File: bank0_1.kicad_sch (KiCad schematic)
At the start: 1 part, among them U1 ECP5-BGA256

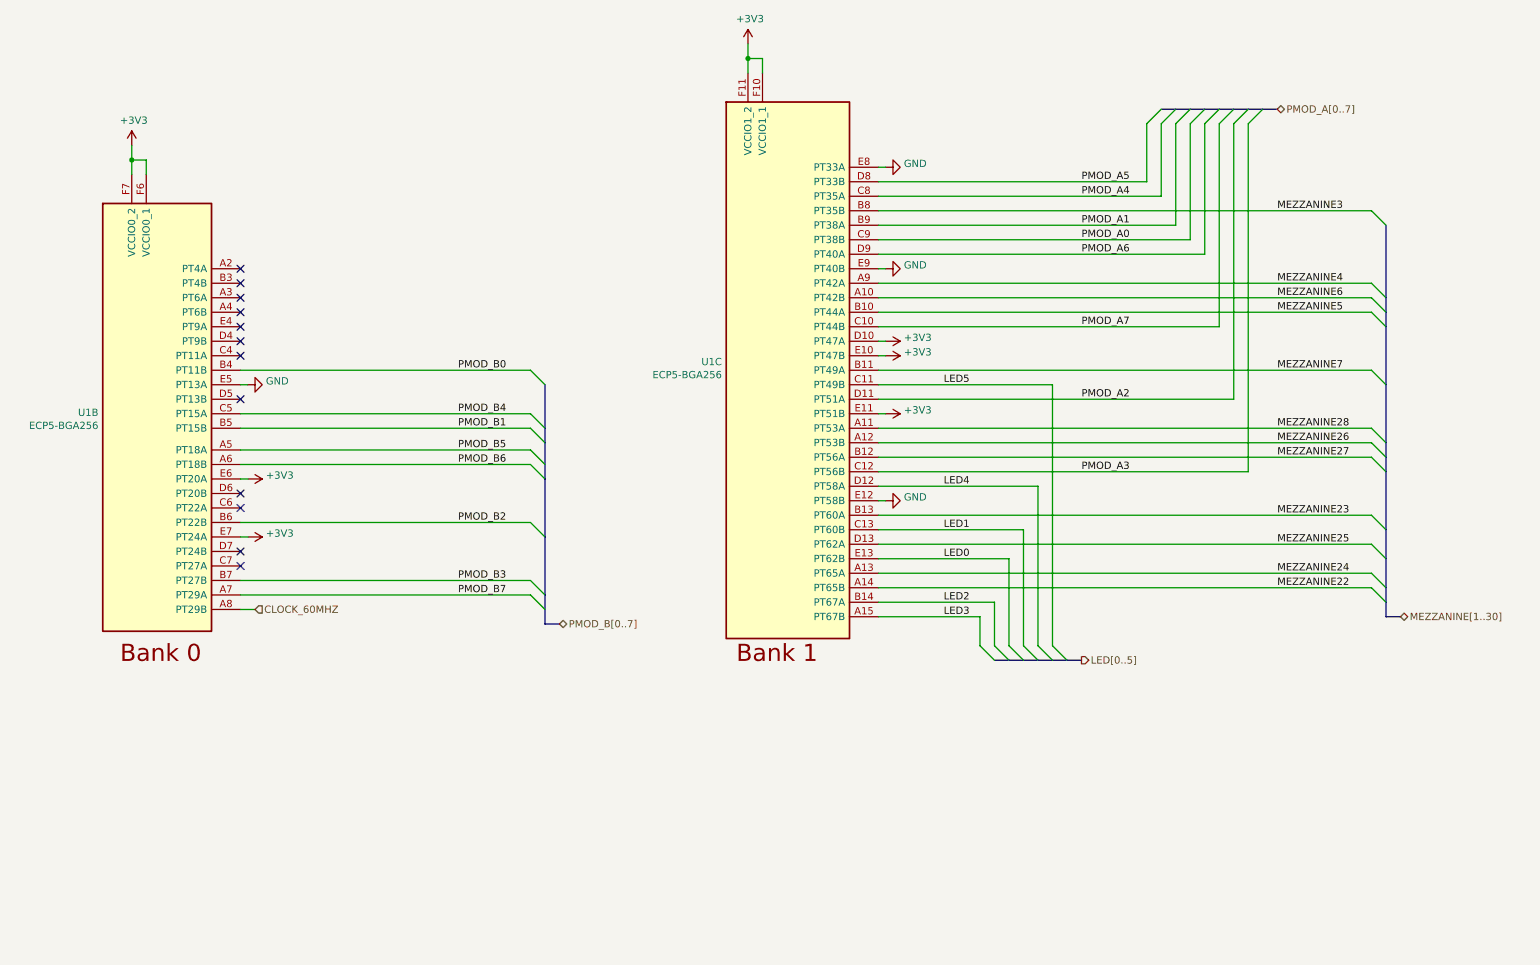
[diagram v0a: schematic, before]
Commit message: Add radio transceiver
Remove Cynthion-specific features
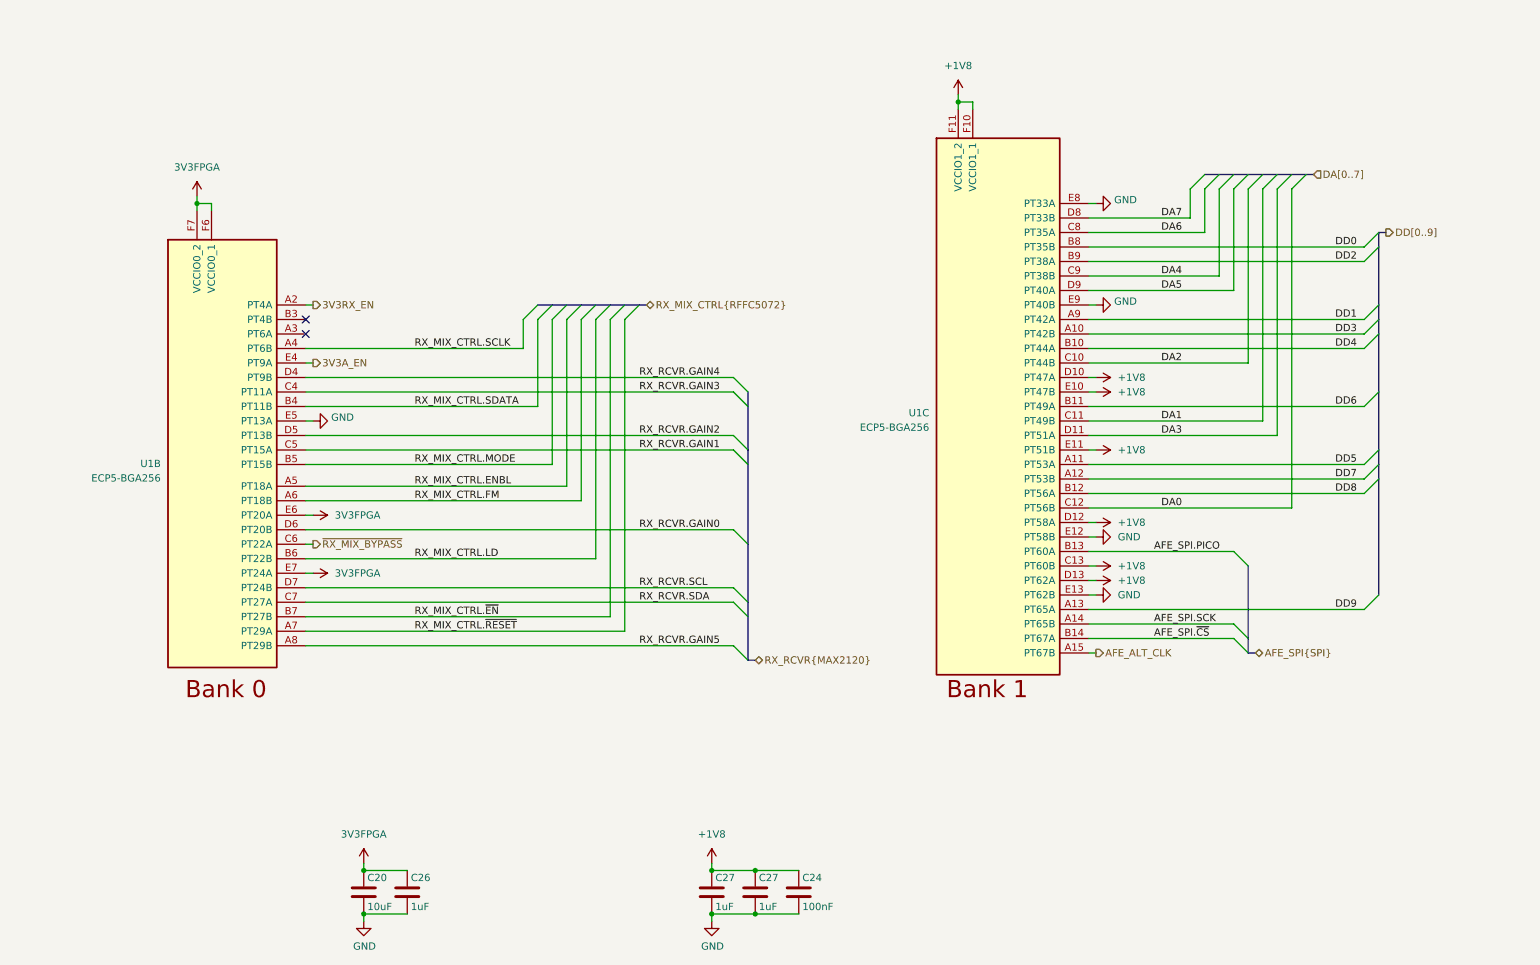
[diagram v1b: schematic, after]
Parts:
- added C20: 10uF, Capacitor_SMD:C_0603_1608Metric, symbol Device:C
- added C24: 100nF, Capacitor_SMD:C_0402_1005Metric, symbol Device:C
- added C26, C27 (x2): 1uF, Capacitor_SMD:C_0402_1005Metric, symbol Device:C
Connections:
- net LED0 is gone; now on net GND: U1.E13 (PT62B)
- net LED1 is gone; now on net +1V8: U1.C13 (PT60B)
- net LED4 is gone; now on net +1V8: U1.D12 (PT58A)
- net MEZZANINE25 is gone; now on net +1V8: U1.D13 (PT62A)
- net GND: now also C20.2, C24.2, C26.2, C27.2, C27.2
- net 3V3RX_EN: now reaches U1.A2 (PT4A)
- net RX_MIX_CTRL.SCLK: now reaches U1.A4 (PT6B)
- net RX_RCVR.GAIN3: now reaches U1.C4 (PT11A)
- net ~{RX_MIX_BYPASS}: now reaches U1.C6 (PT22A)
- net RX_RCVR.SDA: now reaches U1.C7 (PT27A)
- net RX_RCVR.GAIN4: now reaches U1.D4 (PT9B)
- net RX_RCVR.GAIN2: now reaches U1.D5 (PT13B)
- net RX_RCVR.GAIN0: now reaches U1.D6 (PT20B)
- net RX_RCVR.SCL: now reaches U1.D7 (PT24B)
- net 3V3A_EN: now reaches U1.E4 (PT9A)
- net +3V3 renamed +1V8
- net +1V8: now also C24.1, C27.1, C27.1; no longer U1.E6 (PT20A), U1.E7 (PT24A), U1.F6 (VCCIO0_1), U1.F7 (VCCIO0_2)
- net CLOCK_60MHZ renamed RX_RCVR.GAIN5
- net LED2 renamed AFE_SPI.~{CS}
- net LED3 renamed AFE_ALT_CLK
- net LED5 renamed DA1
- net MEZZANINE22 renamed AFE_SPI.SCK
- net MEZZANINE23 renamed AFE_SPI.PICO
- net MEZZANINE24 renamed DD9
- net MEZZANINE26 renamed DD7
- net MEZZANINE27 renamed DD8
- net MEZZANINE28 renamed DD5
- net MEZZANINE3 renamed DD0
- net MEZZANINE4 renamed DD1
- net MEZZANINE5 renamed DD4
- net MEZZANINE6 renamed DD3
- net MEZZANINE7 renamed DD6
- net PMOD_A0 renamed DA4
- net PMOD_A1 renamed DD2
- net PMOD_A2 renamed DA3
- net PMOD_A3 renamed DA0
- net PMOD_A4 renamed DA6
- net PMOD_A5 renamed DA7
- net PMOD_A6 renamed DA5
- net PMOD_A7 renamed DA2
- net PMOD_B0 renamed RX_MIX_CTRL.SDATA
- net PMOD_B1 renamed RX_MIX_CTRL.MODE
- net PMOD_B2 renamed RX_MIX_CTRL.LD
- net PMOD_B3 renamed RX_MIX_CTRL.~{EN}
- net PMOD_B4 renamed RX_RCVR.GAIN1
- net PMOD_B5 renamed RX_MIX_CTRL.ENBL
- net PMOD_B6 renamed RX_MIX_CTRL.FM
- net PMOD_B7 renamed RX_MIX_CTRL.~{RESET}
- new net 3V3FPGA: C20.1, C26.1, U1.E6 (PT20A), U1.E7 (PT24A), U1.F6 (VCCIO0_1), U1.F7 (VCCIO0_2)
- no-connect marks 12 -> 2
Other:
- company: Copyright 2023 Great Scott Gadgets -> ${COPYRIGHT}
- title: URTI Mainboard -> ${TITLE}
- moved on the sheet: U1B, U1C

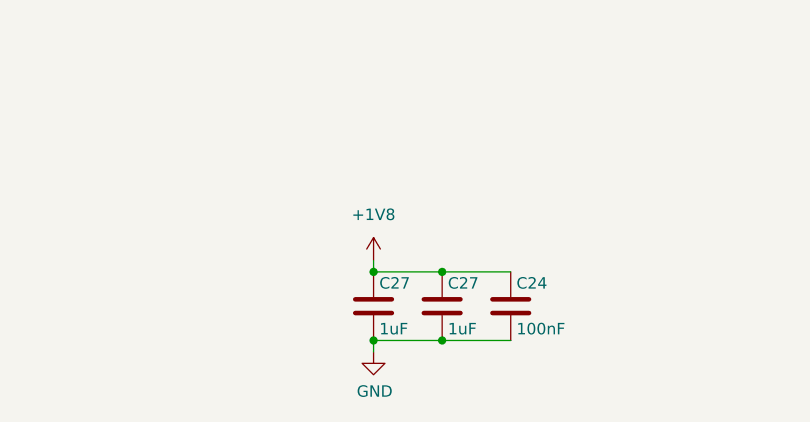
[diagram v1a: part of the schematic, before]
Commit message: Replace open drain clock inverters with push-pull
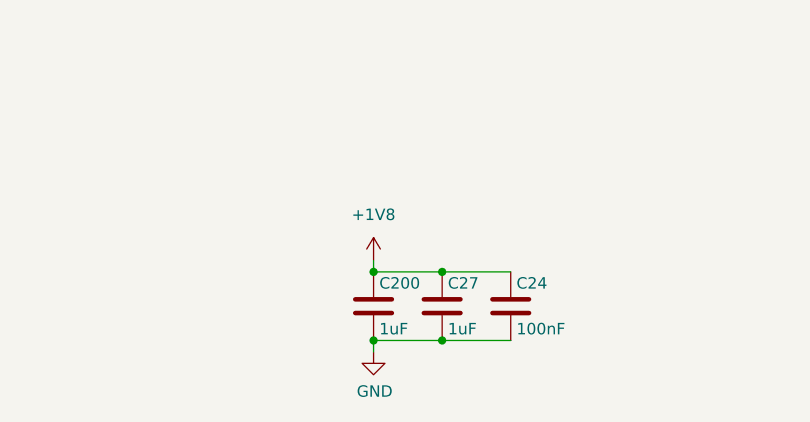
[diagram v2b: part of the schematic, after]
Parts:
- renumbered C27 to C200
